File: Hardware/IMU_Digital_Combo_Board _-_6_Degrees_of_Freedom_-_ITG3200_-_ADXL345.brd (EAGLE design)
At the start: 15.2 x 16.5 mm, 17 parts, among them U1 ADXL345, U3 ITG-32001:1

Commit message: Proper CC 3.0 Attribution
Added proper CC 3.0 attribution in board and schematic.
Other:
- board text added: "A. Weiss"
- board text added: "Revised by: Kade Jensen"
- board text removed: "Kade Jensen"

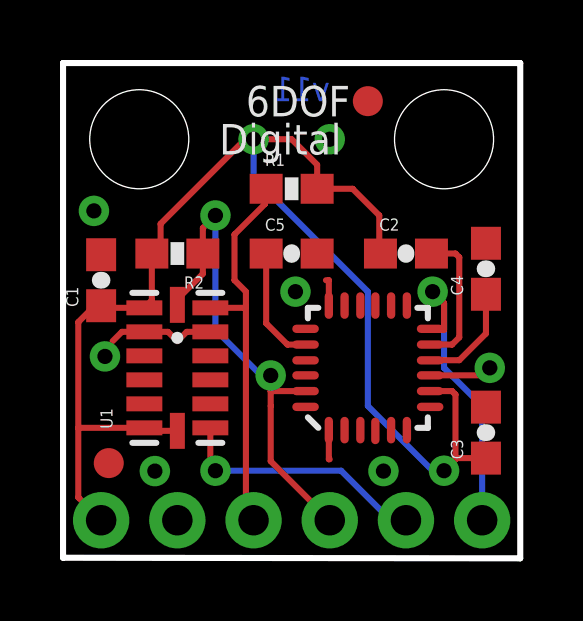
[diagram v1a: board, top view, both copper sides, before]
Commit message: Updated ADXL345 Package and connected SDA signal
SDA trace had gotten dropped in previous design by accident. Reconnected
now and took the opportunity to include new ADXL345 footprint. Had to
change the route job significantly to make it all fit.
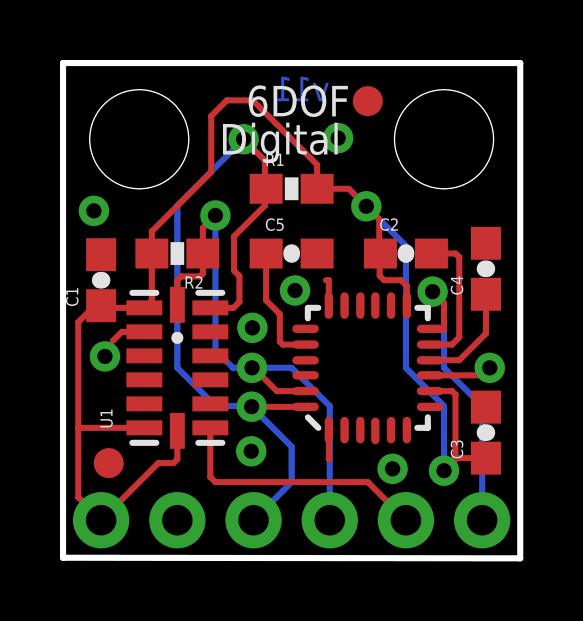
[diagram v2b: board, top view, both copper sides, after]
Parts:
- U1: value ADXL345 -> ADXL3451:1; device SparkFun:LGA14 -> Testing:LGA14
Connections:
- net 3.3V: now also U3.13
- net SDA: now also U3.24
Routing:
- net SDA: track 13.0 -> 25.5 mm, vias 0 -> 2
- net 3.3V: track 46.1 -> 50.0 mm
- net GND: track 12.4 -> 9.99 mm, vias 7 -> 8
- net SCL: track 16.6 -> 18.9 mm
- net INT1: track 8.53 -> 8.76 mm, vias 1 -> 0

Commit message: Rerouted a few traces
Changed  two 3.3V and one of the INT traces for cleaner signal. Moved a
GND via and a fiducial as well.
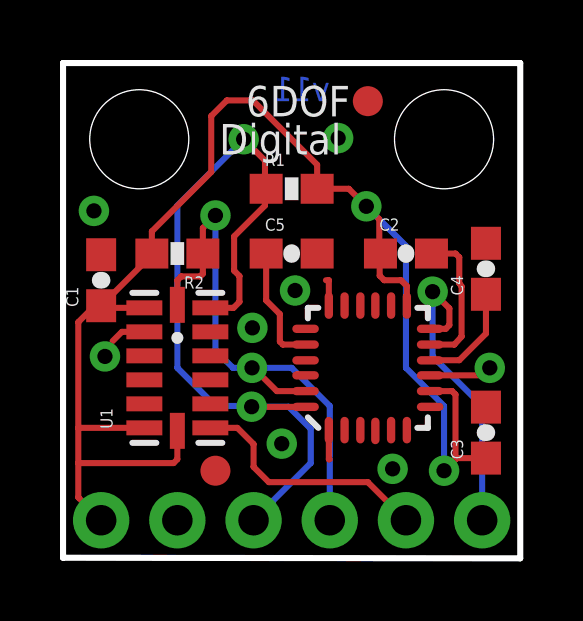
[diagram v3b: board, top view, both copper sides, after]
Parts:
- moved JP6 3.57 mm to (5.08, 2.92)
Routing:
- net SDA: track 25.5 -> 26.8 mm
- net INT1: track 8.76 -> 8.24 mm
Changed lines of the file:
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@@
 <setting verticaltext="up"/>
 </settings>
-<grid distance="0.05" unitdist="inch" unit="inch" style="lines" multiple="1" display="yes" altdistance="0.005" altunitdist="inch" altunit="inch"/>
+<grid distance="0.05" unitdist="inch" unit="inch" style="lines" multiple="1" display="yes" altdistance="0.001" altunitdist="inch" altunit="inch"/>
 <layers>
 <layer number="1" name="Top" color="4" fill="1" visible="yes" active="yes"/>
@@
 <element name="U3" library="Testing" package="QFN-24_ITG3200_1:1" value="ITG-32001:1" x="10.16" y="6.35" rot="R90"/>
 <element name="JP4" library="SparkFun" package="FIDUCIAL-1X2" value="FIDUCIAL1X2" x="10.16" y="15.24"/>
-<element name="JP6" library="SparkFun" package="FIDUCIAL-1X2" value="FIDUCIAL1X2" x="1.524" y="3.175"/>
+<element name="JP6" library="SparkFun" package="FIDUCIAL-1X2" value="FIDUCIAL1X2" x="5.08" y="2.921"/>
 </elements>
 <signals>
@@
 <wire x1="12.28" y1="10.16" x2="13.081" y2="10.16" width="0.2032" layer="1"/>
 <wire x1="13.081" y1="10.16" x2="13.208" y2="10.033" width="0.2032" layer="1"/>
-<wire x1="13.208" y1="10.033" x2="13.208" y2="7.366" width="0.2032" layer="1"/>
 <via x="14.224" y="6.35" extent="1-16" drill="0.508"/>
-<wire x1="12.2362" y1="7.1254" x2="12.9674" y2="7.1254" width="0.2032" layer="1"/>
 <via x="9.1694" y="14.0081" extent="1-16" drill="0.508"/>
-<wire x1="12.9674" y1="7.1254" x2="13.208" y2="7.366" width="0.2032" layer="1"/>
 <wire x1="12.2362" y1="6.1" x2="13.974" y2="6.1" width="0.2032" layer="1"/>
 <wire x1="13.974" y1="6.1" x2="14.224" y2="6.35" width="0.2032" layer="1"/>
 <via x="6.3119" y="7.6835" extent="1-16" drill="0.508"/>
-<via x="6.2738" y="3.5687" extent="1-16" drill="0.508"/>
+<via x="7.2898" y="3.8227" extent="1-16" drill="0.508"/>
+<wire x1="12.2362" y1="7.1254" x2="13.0436" y2="7.1254" width="0.2032" layer="1"/>
+<wire x1="13.0436" y1="7.1254" x2="13.2842" y2="7.3914" width="0.2032" layer="1"/>
+<wire x1="13.2842" y1="7.3914" x2="13.2842" y2="9.0678" width="0.2032" layer="1"/>
+<wire x1="13.2842" y1="9.0678" x2="13.208" y2="9.1694" width="0.2032" layer="1"/>
+<wire x1="13.208" y1="9.1694" x2="13.208" y2="10.033" width="0.2032" layer="1"/>
 </signal>
 <signal name="3.3V">
@@
 <wire x1="0.984" y1="8.35" x2="0.508" y2="7.874" width="0.2032" layer="1"/>
 <wire x1="0.508" y1="7.874" x2="0.508" y2="4.35" width="0.2032" layer="1"/>
-<wire x1="0.508" y1="4.35" x2="0.508" y2="2.032" width="0.2032" layer="1"/>
+<wire x1="0.508" y1="4.35" x2="0.508" y2="3.175" width="0.2032" layer="1"/>
+<wire x1="0.508" y1="3.175" x2="0.508" y2="2.032" width="0.2032" layer="1"/>
 <wire x1="0.508" y1="2.032" x2="1.27" y2="1.27" width="0.2032" layer="1"/>
-<wire x1="2.96" y1="10.16" x2="2.96" y2="8.6" width="0.2032" layer="1"/>
-<wire x1="2.96" y1="8.6" x2="2.71" y2="8.35" width="0.2032" layer="1"/>
 <contactref element="U3" pad="8"/>
 <wire x1="1.27" y1="8.421" x2="1.27" y2="8.35" width="0.2032" layer="1"/>
@@
 <wire x1="3.81" y1="4.25" x2="3.81" y2="3.302" width="0.2032" layer="1"/>
 <wire x1="3.81" y1="3.302" x2="3.683" y2="3.175" width="0.2032" layer="1"/>
-<wire x1="3.683" y1="3.175" x2="3.175" y2="3.175" width="0.2032" layer="1"/>
-<wire x1="3.175" y1="3.175" x2="1.27" y2="1.27" width="0.2032" layer="1"/>
 <wire x1="2.96" y1="10.8975" x2="4.9403" y2="12.8778" width="0.2032" layer="1"/>
 <wire x1="4.9403" y1="12.8778" x2="4.9403" y2="14.7447" width="0.2032" layer="1"/>
@@
 <wire x1="11.43" y1="6.35" x2="11.43" y2="10.414" width="0.2032" layer="16"/>
 <wire x1="11.43" y1="10.414" x2="10.1092" y2="11.7348" width="0.2032" layer="16"/>
+<wire x1="3.683" y1="3.175" x2="0.508" y2="3.175" width="0.2032" layer="1"/>
+<wire x1="2.96" y1="10.16" x2="2.96" y2="10.111" width="0.2032" layer="1"/>
+<wire x1="2.96" y1="10.111" x2="1.27" y2="8.421" width="0.2032" layer="1"/>
 </signal>
 <signal name="SCL">
@@
 <wire x1="3.81" y1="6.35" x2="3.81" y2="11.7602" width="0.2032" layer="16"/>
 <wire x1="6.0198" y1="13.97" x2="3.81" y2="11.7602" width="0.2032" layer="16"/>
-<wire x1="6.35" y1="1.27" x2="7.62" y2="2.54" width="0.2032" layer="16"/>
 <wire x1="5.08" y1="5.08" x2="6.2611" y2="5.08" width="0.2032" layer="16"/>
 <wire x1="6.2611" y1="5.08" x2="6.2865" y2="5.0546" width="0.2032" layer="16"/>
 <wire x1="8.0838" y1="5.0492" x2="6.2919" y2="5.0492" width="0.2032" layer="1"/>
 <wire x1="6.2919" y1="5.0492" x2="6.2865" y2="5.0546" width="0.2032" layer="1"/>
-<wire x1="7.62" y1="2.54" x2="7.62" y2="3.7211" width="0.2032" layer="16"/>
-<wire x1="7.62" y1="3.7211" x2="6.2865" y2="5.0546" width="0.2032" layer="16"/>
+<wire x1="6.2865" y1="5.0546" x2="7.5184" y2="5.0546" width="0.2032" layer="16"/>
+<wire x1="7.5184" y1="5.0546" x2="8.255" y2="4.318" width="0.2032" layer="16"/>
+<wire x1="8.255" y1="4.318" x2="8.255" y2="3.175" width="0.2032" layer="16"/>
+<wire x1="8.255" y1="3.175" x2="6.35" y2="1.27" width="0.2032" layer="16"/>
 </signal>
 <signal name="INT1">
@@
 <contactref element="JP1" pad="5"/>
 <wire x1="10.16" y1="2.54" x2="11.43" y2="1.27" width="0.2032" layer="1"/>
-<wire x1="4.91" y1="4.35" x2="4.91" y2="2.71" width="0.2032" layer="1"/>
-<wire x1="4.91" y1="2.71" x2="5.08" y2="2.54" width="0.2032" layer="1"/>
-<wire x1="5.08" y1="2.54" x2="10.16" y2="2.54" width="0.2032" layer="1"/>
+<wire x1="4.91" y1="4.35" x2="5.81" y2="4.35" width="0.2032" layer="1"/>
+<wire x1="10.16" y1="2.54" x2="6.858" y2="2.54" width="0.2032" layer="1"/>
+<wire x1="5.81" y1="4.35" x2="6.35" y2="3.81" width="0.2032" layer="1"/>
+<wire x1="6.35" y1="3.81" x2="6.35" y2="3.048" width="0.2032" layer="1"/>
+<wire x1="6.35" y1="3.048" x2="6.858" y2="2.54" width="0.2032" layer="1"/>
 </signal>
 <signal name="N$2">
@@
 <wire x1="13.97" y1="5.08" x2="13.97" y2="1.27" width="0.2032" layer="16"/>
 <contactref element="U3" pad="12"/>
-<wire x1="13.97" y1="5.08" x2="12.7" y2="6.35" width="0.2032" layer="16"/>
+<wire x1="13.97" y1="5.08" x2="12.319" y2="6.731" width="0.2032" layer="16"/>
 <via x="12.319" y="8.89" extent="1-16" drill="0.508"/>
-<wire x1="12.7" y1="7.62" x2="12.267" y2="7.62" width="0.2032" layer="1"/>
 <wire x1="12.267" y1="7.62" x2="12.2362" y2="7.6508" width="0.2032" layer="1"/>
-<wire x1="12.7" y1="7.62" x2="12.7" y2="8.509" width="0.2032" layer="1"/>
-<wire x1="12.7" y1="8.509" x2="12.319" y2="8.89" width="0.2032" layer="1"/>
-<wire x1="12.7" y1="6.35" x2="12.7" y2="8.509" width="0.2032" layer="16"/>
-<wire x1="12.7" y1="8.509" x2="12.319" y2="8.89" width="0.2032" layer="16"/>
+<wire x1="12.2362" y1="7.6508" x2="12.7562" y2="7.6508" width="0.2032" layer="1"/>
+<wire x1="12.7562" y1="7.6508" x2="12.8778" y2="7.7724" width="0.2032" layer="1"/>
+<wire x1="12.8778" y1="7.7724" x2="12.8778" y2="8.3312" width="0.2032" layer="1"/>
+<wire x1="12.8778" y1="8.3312" x2="12.319" y2="8.89" width="0.2032" layer="1"/>
+<wire x1="12.319" y1="8.89" x2="12.319" y2="6.731" width="0.2032" layer="16"/>
 </signal>
 </signals>

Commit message: Updating README,  cleaning up board files, adding library
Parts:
- added FRAME1: FRAME-LETTER, SparkFun-Aesthetics:CREATIVE_COMMONS
- U$1: value CREATIVE_COMMONS -> REVISION; device SparkFun:CREATIVE_COMMONS -> SparkFun-Aesthetics:REVISION
- moved U$1 7.18 mm to (-1.27, -12.7)
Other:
- board text added: "Aaron Weiss"
- board text added: "Kade Jensen"
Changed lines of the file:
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@@
 <?xml version="1.0" encoding="utf-8"?>
 <!DOCTYPE eagle SYSTEM "eagle.dtd">
-<eagle version="6.4">
+<eagle version="6.5.0">
 <drawing>
 <settings>
@@
 <setting verticaltext="up"/>
 </settings>
-<grid distance="0.05" unitdist="inch" unit="inch" style="lines" multiple="1" display="yes" altdistance="0.001" altunitdist="inch" altunit="inch"/>
+<grid distance="0.05" unitdist="inch" unit="inch" style="lines" multiple="1" display="yes" altdistance="0.005" altunitdist="inch" altunit="inch"/>
 <layers>
 <layer number="1" name="Top" color="4" fill="1" visible="yes" active="yes"/>
@@
 <layer number="47" name="Measures" color="7" fill="1" visible="no" active="yes"/>
 <layer number="48" name="Document" color="7" fill="1" visible="no" active="yes"/>
-<layer number="49" name="Reference" color="7" fill="1" visible="yes" active="yes"/>
+<layer number="49" name="Reference" color="7" fill="1" visible="no" active="yes"/>
 <layer number="50" name="dxf" color="7" fill="1" visible="no" active="yes"/>
 <layer number="51" name="tDocu" color="6" fill="1" visible="yes" active="yes"/>
@@
 <rectangle x1="3.429" y1="5.715" x2="3.81" y2="6.096" layer="41"/>
 <rectangle x1="2.6035" y1="5.461" x2="2.8194" y2="5.6261" layer="41"/>
+<text x="13.97" y="-8.89" size="1.778" layer="51" font="vector" ratio="15">Aaron Weiss</text>
+<text x="13.97" y="-12.7" size="1.778" layer="51" font="vector" ratio="15">Kade Jensen</text>
 </plain>
 <attributes>
@@
 <element name="C4" library="SparkFun" package="0603-CAP" value="0.1uF" x="14.097" y="9.652" rot="R90"/>
 <element name="C5" library="SparkFun" package="0603-CAP" value="2.2nF" x="7.62" y="10.16"/>
-<element name="U$1" library="SparkFun" package="CREATIVE_COMMONS" value="CREATIVE_COMMONS" x="-6.35" y="-7.62"/>
 <element name="JP3" library="SparkFun" package="SFE-LOGO-FLAME" value="LOGO-SFESK" x="13.5128" y="7.62" rot="MR0"/>
 <element name="JP1" library="SparkFun" package="1X06" value="" x="1.27" y="1.27" rot="MR180"/>
@@
 <element name="JP4" library="SparkFun" package="FIDUCIAL-1X2" value="FIDUCIAL1X2" x="10.16" y="15.24"/>
 <element name="JP6" library="SparkFun" package="FIDUCIAL-1X2" value="FIDUCIAL1X2" x="5.08" y="2.921"/>
+<element name="FRAME1" library="SparkFun-Aesthetics" package="CREATIVE_COMMONS" value="FRAME-LETTER" x="-13.189478125" y="-8.89"/>
+<element name="U$1" library="SparkFun-Aesthetics" package="REVISION" value="REVISION" x="-1.27" y="-12.7"/>
 </elements>
 <signals>
